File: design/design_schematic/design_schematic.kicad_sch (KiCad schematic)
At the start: 22 parts, among them U1 nRF52840, X1 32MHz

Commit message: add power management
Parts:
- added C10, C13, C17, C9: 4.7uF, ScottoKeebs_Components:Capacitor_0402, symbol Device:C_Small
- added IC1: XC9291B33D0R-G, XC9290A07E0RG, symbol SamacSys_Parts:XC9291B33D0R-G
- added J1: USB_C_Receptacle_USB2.0_16P, Connector_USB:USB_C_Receptacle_HRO_TYPE-C-31-M-12, symbol Connector:USB_C_Receptacle_USB2.0_16P
- added J2: Battery Pos, symbol Connector_Generic:Conn_01x01
- added J3: Battery Neg, symbol Connector_Generic:Conn_01x01
- added L5: 1uH, symbol Device:L
- added R1, R2: 5k1, symbol Device:R
- added R3: 3k, symbol Device:R
- added R4: 1k8, symbol Device:R
- added R5, R6: 10k, symbol Device:R
- added U2: BQ24072RGT, Package_DFN_QFN:VQFN-16-1EP_3x3mm_P0.5mm_EP1.6x1.6mm, symbol Battery_Management:BQ24072RGT
- added U3: USB6B1, Package_SO:SOIC-8_3.9x4.9mm_P1.27mm, symbol Power_Protection:USB6B1
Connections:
- net GND: now also C10.1, C13.1, C17.2, C9.2, IC1.3 (GND), J1.A1 (GND), J1.A12 (GND), J1.B1 (GND), J1.B12 (GND), J3.1 (Pin_1), R1.2, R2.2, R3.1, R4.2, R5.1, U2.15 (TD), U2.17 (VSS), U2.4 (~{CE}), U2.5 (EN2), U2.8 (VSS), U3.4 (GND), U3.5 (GND)
- net VBUS: now also C13.2, IC1.4 (VOUT), L5.1
- new net: C17.1, J2.1 (Pin_1), U2.2 (BAT), U2.3 (BAT)
- new net: J1.B5 (CC2), R2.1
- new net: C9.1, J1.A4 (VBUS), J1.A9 (VBUS), J1.B4 (VBUS), J1.B9 (VBUS), U2.13 (IN), U2.6 (EN1), U3.1 (VBUS), U3.8 (VBUS)
- new net: J1.A7 (D-), J1.B7 (D-), U3.2 (I/O1)
- new net: J1.A6 (D+), J1.B6 (D+), U3.3 (I/O2)
- new net: C10.2, IC1.1 (EN), IC1.2 (VIN), R6.1, U2.10 (OUT), U2.11 (OUT)
- new net: IC1.5 (LX), L5.2
- new net: R4.1, U2.16 (ISET)
- new net: R5.2, U2.1 (TS)
- new net: J1.A5 (CC1), R1.1
- new net: R3.2, U2.12 (ILIM)
- new net CHG: R6.2, U2.9 (~{CHG})
- new net D+: U3.6 (I/O2)
- new net D-: U3.7 (I/O1)
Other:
- note added: "5V input and variable battery input changeed to 3.3V output using 3.3V DC-DC Converter. Max. Current set to 500mA to match USB."
- note added: "BLE Enabled"
- note added: "Contains USB C, ESD Protection, Battery charging and DC-DC conversion to 3.3V"
- note added: "Power Management"

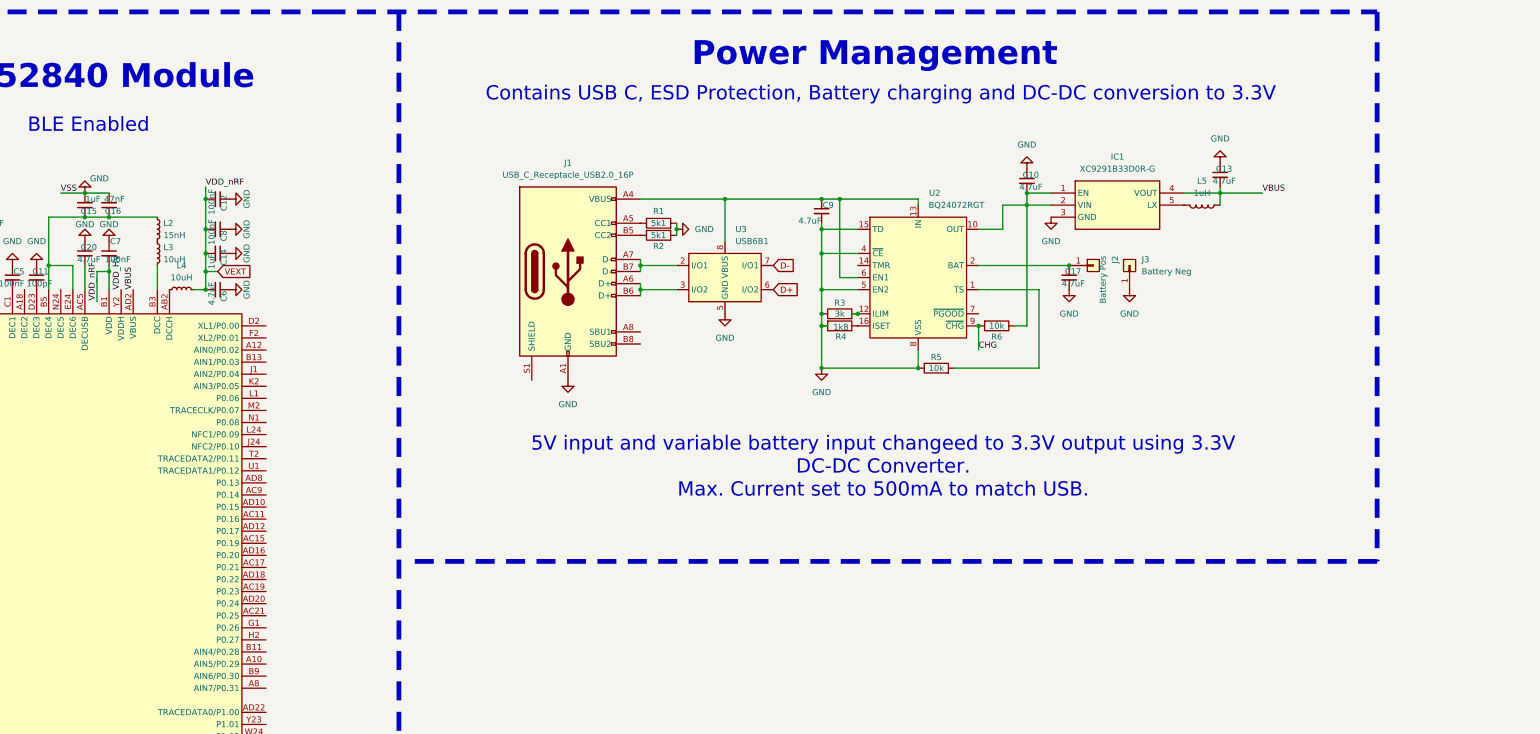
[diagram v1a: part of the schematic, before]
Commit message: complete power management
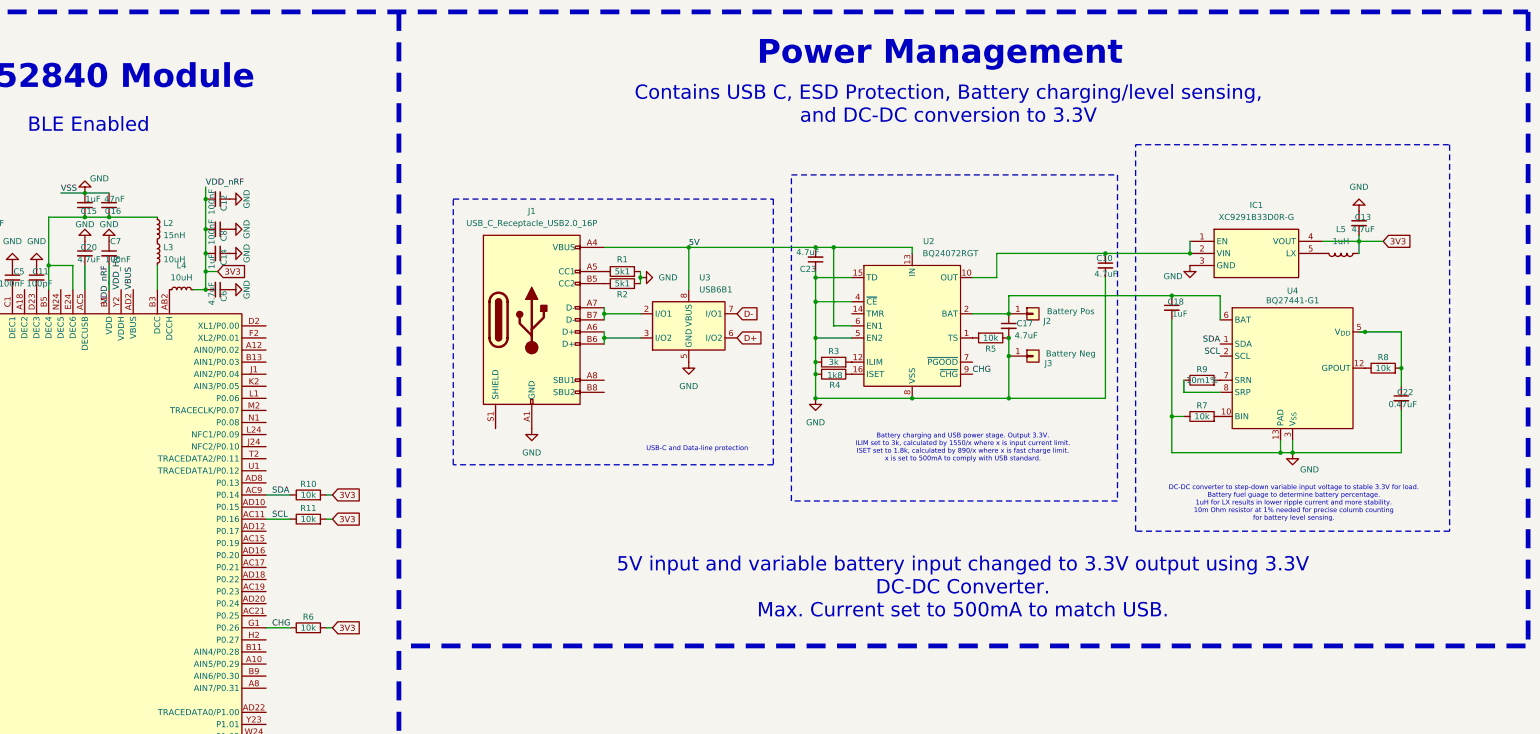
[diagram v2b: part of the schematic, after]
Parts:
- removed C9: 4.7uF, ScottoKeebs_Components:Capacitor_0402, symbol Device:C_Small
- added C18: 1uF, ScottoKeebs_Components:Capacitor_0402, symbol Device:C_Small
- added C22: 0.47uF, ScottoKeebs_Components:Capacitor_0402, symbol Device:C_Small
- added C23: 4.7uF, ScottoKeebs_Components:Capacitor_0402, symbol Device:C_Small
- added R10, R11, R7, R8: 10k, symbol Device:R
- added R9: 10m1%, symbol Device:R
- added U4: BQ27441-G1, Package_SON:Texas_S-PDSO-N12, symbol Battery_Management:BQ27441-G1
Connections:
- net CHG: now also R6.1, U1.G1 (P0.26); no longer R6.2
- net GND: now also C10.2, C18.2, C22.2, C23.1, R7.1, U4.13 (PAD), U4.3 (V_{SS}); no longer C10.1
- net VBUS: no longer C13.2, IC1.4 (VOUT), L5.1
- net at C17.1, J2.1 (Pin_1), U2.2 (BAT)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: now also C18.1, U4.6 (BAT)
- net SCL: now reaches U1.AC11 (P0.16)
- net SCL: now also R11.1, U4.2 (SCL)
- net SDA: now reaches U1.AC9 (P0.14)
- net SDA: now also R10.1, U4.1 (SDA)
- net 5V: now reaches J1.A4 (VBUS), J1.A9 (VBUS), J1.B4 (VBUS), J1.B9 (VBUS), U2.13 (IN), U2.6 (EN1), U3.1 (VBUS), U3.8 (VBUS)
- net 5V: now also C23.2
- net at IC1.1 (EN), IC1.2 (VIN), U2.10 (OUT)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: now also C10.1; no longer C10.2, R6.1
- net VEXT renamed 3V3
- net 3V3: now also C13.2, IC1.4 (VOUT), L5.1, R6.2, R10.2, R11.2
- new net: R7.2, U4.10 (BIN)
- new net: R8.1, U4.12 (GPOUT)
- new net: C22.1, R8.2, U4.5 (V_{DD})
- new net: R9.2, U4.7 (SRN)
- new net: R9.1, U4.8 (SRP)
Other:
- note added: "5V input and variable battery input changed to 3.3V output using 3.3V DC-DC Converter. Max. Current set to 500mA to match USB."
- note added: "Battery charging and USB power stage. Output 3.3V. ILIM set to 3k, calculated by 1550/x where x is input current limit. ISET set to 1.8k, calculated by 890/x where x is fast charge limit. x is set to 500mA to comply with USB standard."
- note added: "Contains USB C, ESD Protection, Battery charging/level sensing, and DC-DC conversion to 3.3V"
- note added: "DC-DC converter to step-down variable input voltage to stable 3.3V for load. Battery fuel guage to determine battery percentage. 1uH for LX results in lower ripple current and more stability. 10m Ohm resistor at 1% needed for precise columb counting for battery level sensing."
- note added: "USB-C and Data-line protection"
- note removed: "5V input and variable battery input changeed to 3.3V output using 3.3V DC-DC Converter. Max. Current set to 500mA to match USB."
- note removed: "Contains USB C, ESD Protection, Battery charging and DC-DC conversion to 3.3V"
- moved on the sheet: C10, C13, C17, IC1, J1, J2, J3, L5, R1, R2, R3, R4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

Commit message: begin adding peripherals
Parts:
- added C9: 4.7uF, ScottoKeebs_Components:Capacitor_0402, symbol Device:C_Small
- added J4: OLED_128x32, ScottoKeebs_Components:OLED_128x32, symbol ScottoKeebs:OLED_128x32
- added U5, U6: PEC11L-4015F-S0015, PEC11L4015FS0015, symbol SamacSys_Parts:PEC11L-4015F-S0015
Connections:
- net 3V3: now also J4.2 (VCC)
- net GND: now also C9.2, U5.1 (COM), U5.B1 (WIPER), U6.1 (COM), U6.B1 (WIPER)
- net SCL: now also J4.3 (SCL)
- net SDA: now also J4.4 (SDA)
- net NO2: now reaches U1.A10 (AIN5/P0.29)
- net NO2: now also U6.2 (NO)
- net NO: now reaches U1.A8 (AIN7/P0.31)
- net NO: now also U5.2 (NO)
- net CCW: now reaches U1.B15 (P1.14)
- net CCW: now also U5.A1 (CCW)
- net CW: now reaches U1.B17 (P1.12)
- net CW: now also U5.C1 (CW)
- net CCW2: now reaches U1.V23 (P1.03)
- net CCW2: now also U6.A1 (CCW)
- net CW2: now reaches U1.W24 (P1.02)
- net CW2: now also U6.C1 (CW)
- new net: C9.1, J4.1 (GND)
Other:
- note added: "EC11 Encoders, OLED and Cirque glidepoint trackpad"
- note added: "Peripherals"

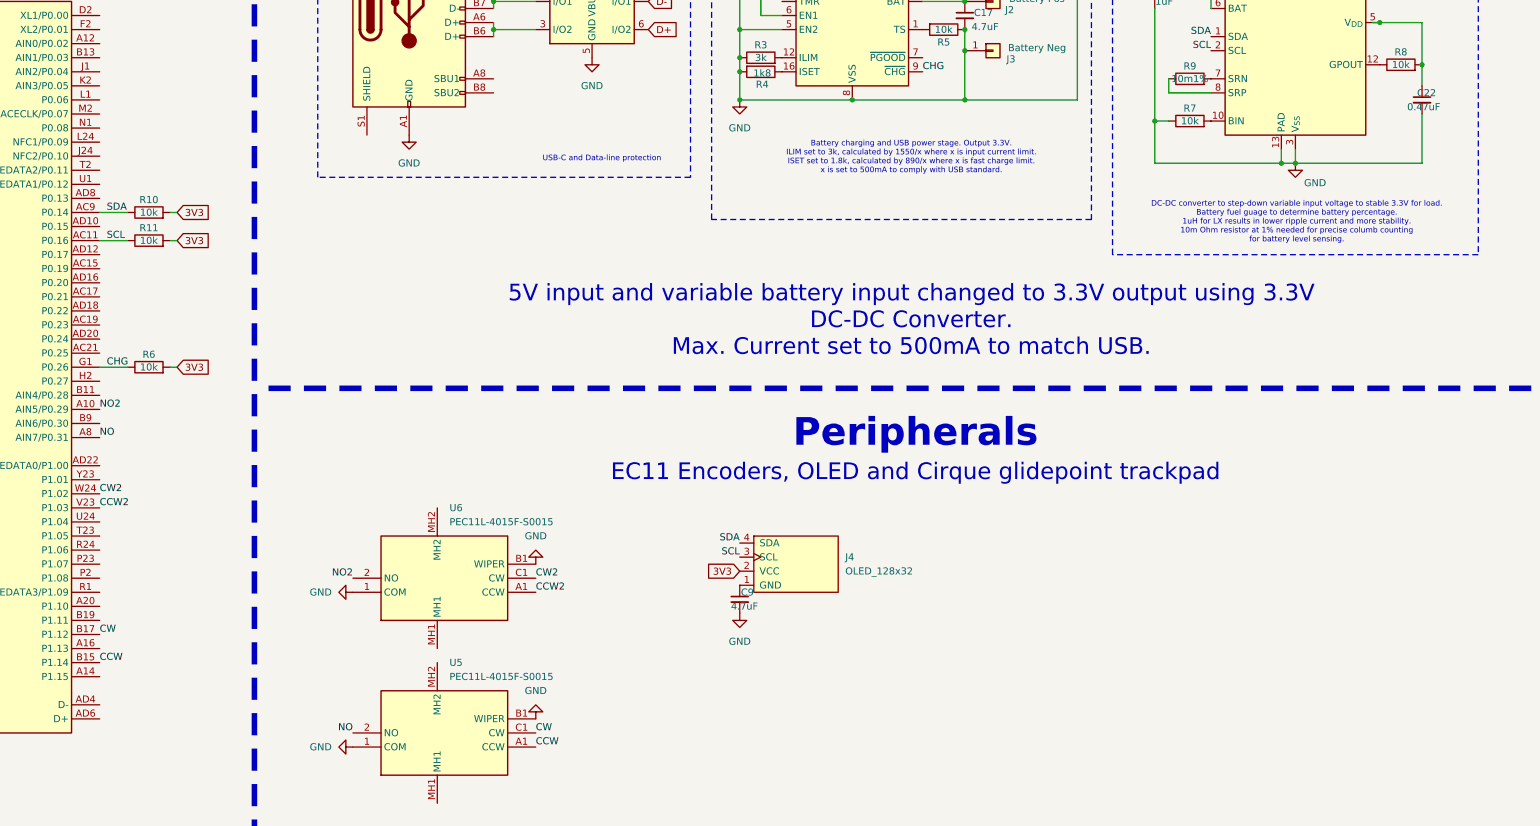
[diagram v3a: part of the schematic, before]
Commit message: add peripherals
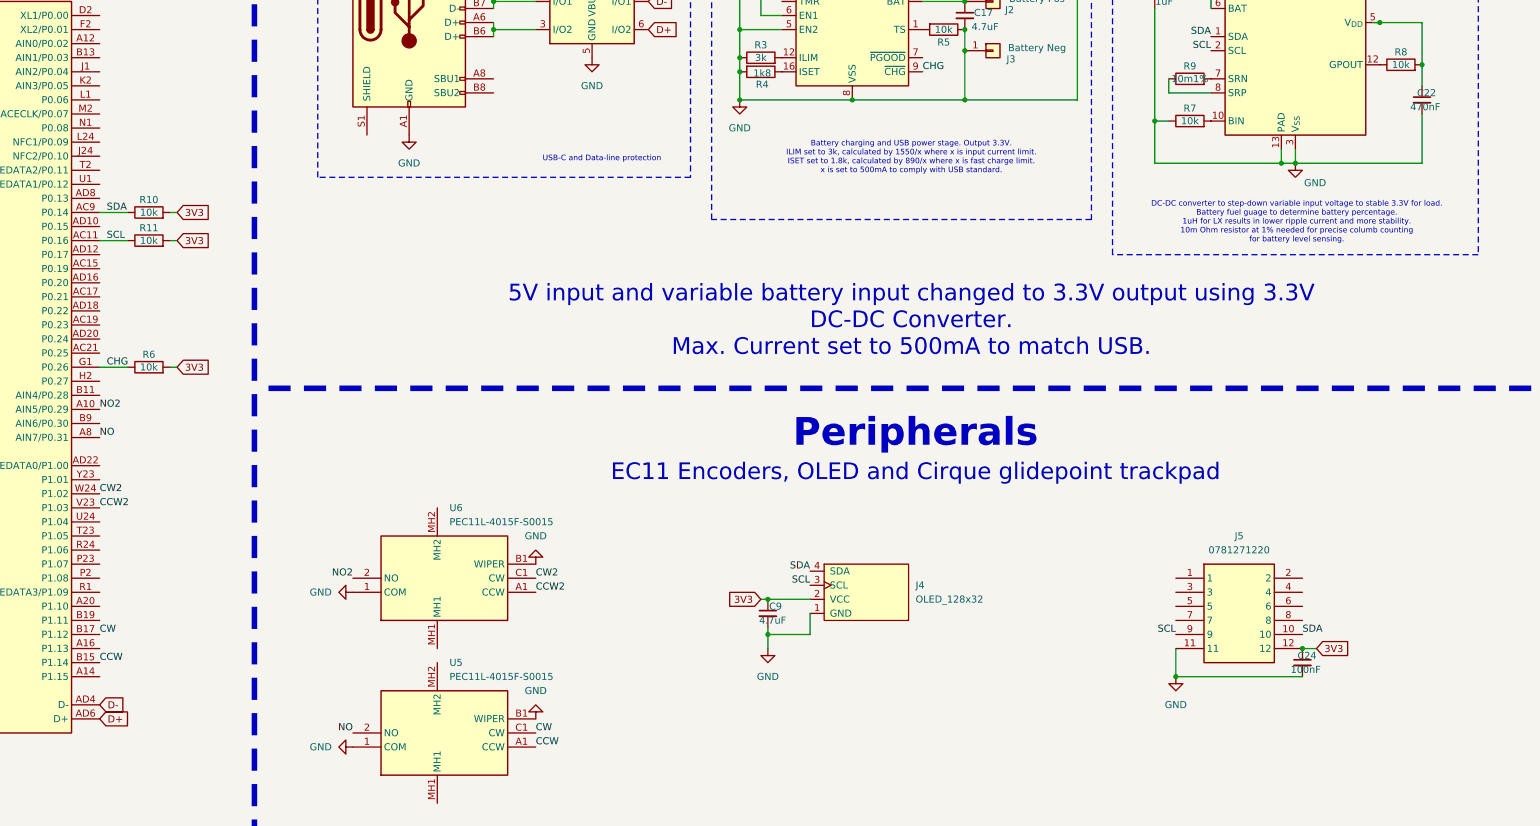
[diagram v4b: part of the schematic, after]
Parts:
- added C24: 100nF, ScottoKeebs_Components:Capacitor_0402, symbol Device:C_Small
- added J5: 0781271220, 0781271220, symbol SamacSys_Parts:0781271220
- C22: value 0.47uF -> 470nF
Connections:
- net 3V3: now also C9.1, C24.1, J5.12
- net D+: now also U1.AD6 (D+)
- net D-: now also U1.AD4 (D-)
- net GND: now also J4.1 (GND), C24.2, J5.11
- net SCL: now also J5.9
- net SDA: now also J5.10
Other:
- moved on the sheet: J4
